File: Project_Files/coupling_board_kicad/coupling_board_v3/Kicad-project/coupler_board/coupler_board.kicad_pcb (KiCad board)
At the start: 2 copper layers, 59.9 x 70 mm, 26 parts, among them IC1 ISO6741DWR, IC2 ISO6740FDWR, IC3 ISO6740FDWR, J1 Molex Microfit, J2 Conn_02x12_Odd_Even, J3 Molex6, J5 DB25_Socket, J7 Molex Microfit, J8 Molex Microfit, J9 Molex Microfit

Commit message: Updated design, added digikey bom
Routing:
- net GND1: vias 2 -> 7

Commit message: Updated design
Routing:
- net Vin: track 60.3 -> 60.8 mm
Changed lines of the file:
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@@
 		(start 100.872 82.296)
 		(end 102.104 83.528)
-		(width 0.508)
+		(width 0.254)
 		(layer "B.Cu")
 		(net 38)
@@
 		(start 104.864 83.528)
 		(end 106.553 85.217)
-		(width 0.508)
+		(width 0.254)
 		(layer "B.Cu")
 		(net 38)
@@
 		(start 102.104 83.528)
 		(end 104.864 83.528)
-		(width 0.508)
+		(width 0.254)
 		(layer "B.Cu")
 		(net 38)
@@
 		(start 103.848 80.988)
 		(end 106.807 83.947)
-		(width 0.508)
+		(width 0.254)
 		(layer "B.Cu")
 		(net 40)
@@
 		(start 102.104 80.988)
 		(end 103.848 80.988)
-		(width 0.508)
+		(width 0.254)
 		(layer "B.Cu")
 		(net 40)
@@
 		(start 100.872 79.756)
 		(end 102.104 80.988)
-		(width 0.508)
+		(width 0.254)
 		(layer "B.Cu")
 		(net 40)
@@
 		(start 100.872 72.136)
 		(end 102.104 73.368)
-		(width 0.508)
+		(width 0.254)
 		(layer "B.Cu")
 		(net 41)
@@
 		(start 102.104 73.368)
 		(end 106.21 73.368)
-		(width 0.508)
+		(width 0.254)
 		(layer "B.Cu")
 		(net 41)
@@
 		(start 102.104 75.908)
 		(end 104.432 75.908)
-		(width 0.508)
+		(width 0.254)
 		(layer "B.Cu")
 		(net 44)
@@
 		(start 100.872 74.676)
 		(end 102.104 75.908)
-		(width 0.508)
+		(width 0.254)
 		(layer "B.Cu")
 		(net 44)
@@
 	)
 	(segment
+		(start 91.765999 81.630001)
+		(end 95.092001 81.630001)
+		(width 3.048)
+		(layer "F.Cu")
+		(net 47)
+	)
+	(segment
+		(start 96.8248 83.3628)
+		(end 96.8248 91.6432)
+		(width 3.048)
+		(layer "F.Cu")
+		(net 47)
+	)
+	(segment
 		(start 91.765999 93.822001)
 		(end 83.614001 93.822001)
@@
 	)
 	(segment
+		(start 94.645999 93.822001)
+		(end 91.765999 93.822001)
+		(width 3.048)
+		(layer "F.Cu")
+		(net 47)
+	)
+	(segment
 		(start 82.742399 80.873303)
 		(end 82.742399 74.999604)
@@
 	)
 	(segment
-		(start 96.1614 92.3066)
-		(end 94.645999 93.822001)
-		(width 3.048)
-		(layer "F.Cu")
-		(net 47)
-	)
-	(segment
 		(start 83.529798 81.660702)
 		(end 91.735298 81.660702)
@@
 	)
 	(segment
-		(start 94.645999 93.822001)
-		(end 91.765999 93.822001)
-		(width 3.048)
-		(layer "F.Cu")
-		(net 47)
-	)
-	(segment
-		(start 91.765999 81.630001)
-		(end 95.092001 81.630001)
-		(width 3.048)
-		(layer "F.Cu")
-		(net 47)
-	)
-	(segment
 		(start 83.529798 81.660702)
 		(end 82.742399 80.873303)
@@
 	)
 	(segment
-		(start 95.092001 81.630001)
-		(end 96.1614 82.6994)
-		(width 3.048)
-		(layer "F.Cu")
-		(net 47)
-	)
-	(segment
 		(start 82.742399 74.999604)
 		(end 83.430001 74.312002)
@@
 	)
 	(segment
-		(start 96.1614 82.6994)
-		(end 96.1614 92.3066)
-		(width 3.048)
-		(layer "F.Cu")
+		(start 96.8248 91.6432)
+		(end 94.645999 93.822001)
+		(width 3.048)
+		(layer "F.Cu")
+		(net 47)
+	)
+	(segment
+		(start 95.092001 81.630001)
+		(end 96.8248 83.3628)
+		(width 3.048)
+		(layer "F.Cu")

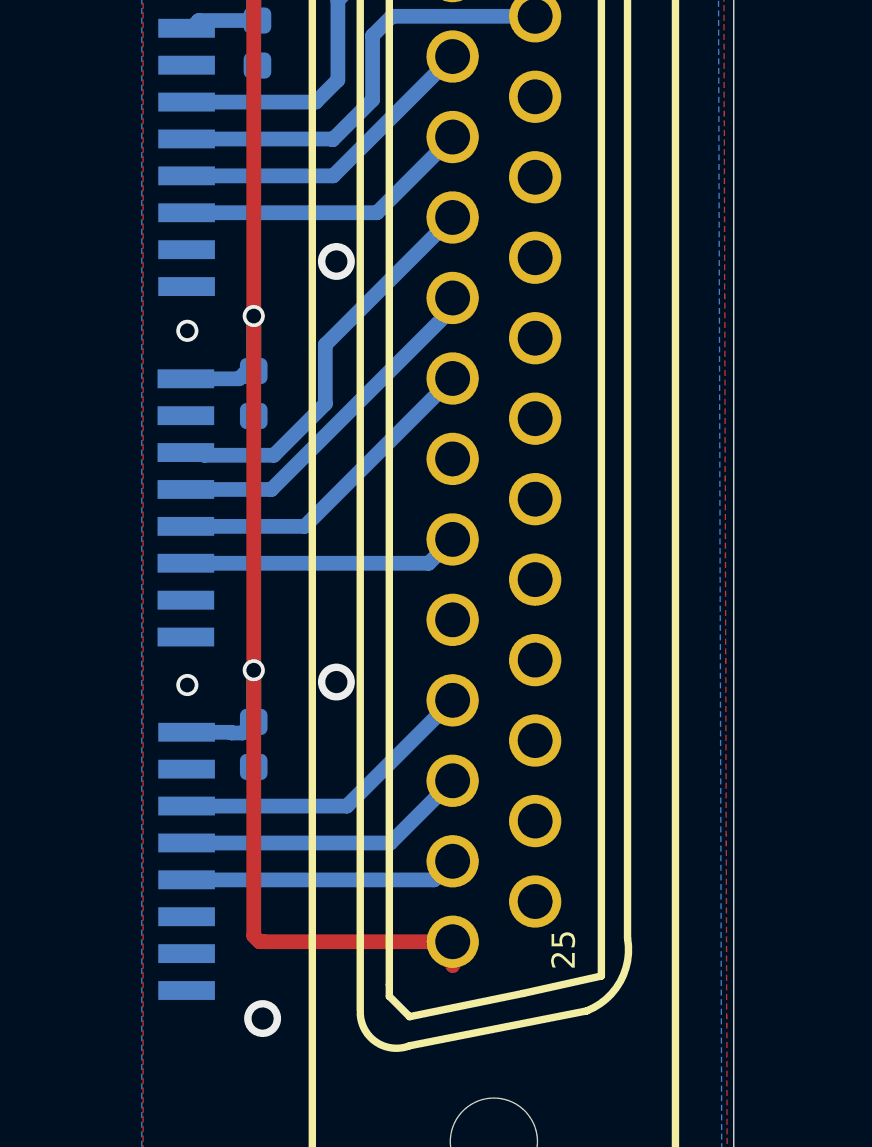
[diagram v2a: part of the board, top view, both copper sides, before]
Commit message: Committing prototyped DRC checked version
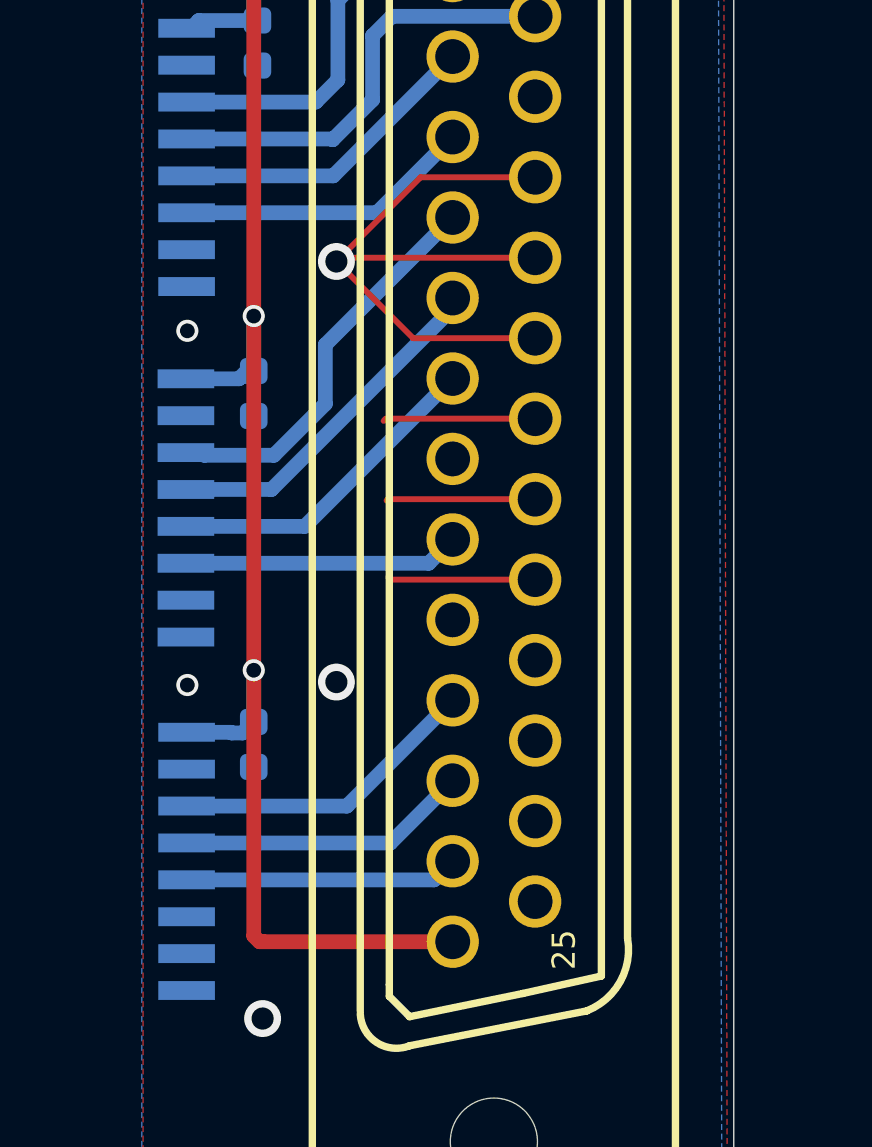
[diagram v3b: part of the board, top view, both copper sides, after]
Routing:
- net GND1: track 0.00 -> 38.3 mm
- net VDD: track 53.7 -> 52.9 mm
